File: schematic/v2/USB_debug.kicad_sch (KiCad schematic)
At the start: 16 parts, among them J25 USB_A, J26 APM_DBG, U19 CH340G, Y5 Crystal

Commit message: time to start routing?
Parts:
- removed Y5: Crystal, symbol Device:Crystal
- added Y2: 12MHz, Crystal:Crystal_HC49-4H_Vertical, symbol Device:Crystal
- J26: value APM_DBG -> UART_DEBUG
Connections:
- net at C24.1, U19.7 (XI): now also Y2.1
- net D-: now reaches J25.2 (D-), U19.6 (UD-)
- net D+: now reaches J25.3 (D+), U19.5 (UD+)
- net at C23.1, U19.8 (XO): now also Y2.2
- net APM_DBG_RX renamed USB_DBG_RX
- net USB_DBG_RX: no longer R80.1, R81.1, U19.2 (TXD)
- net APM_DBG_TX renamed DBG_TX
- net DBG_TX: now also R81.1; no longer R81.2
- net APM_VDD renamed USB_DBG_VDD
- new net USB_DBG_TX: R80.1, R81.2, U19.2 (TXD)
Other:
- note added: "UART -> USB Debug Port"
- note added: "USB2.0 DBG PORT"
- note removed: "APM Debug Port"
- note removed: "APM USB2.0 DBG PORT"

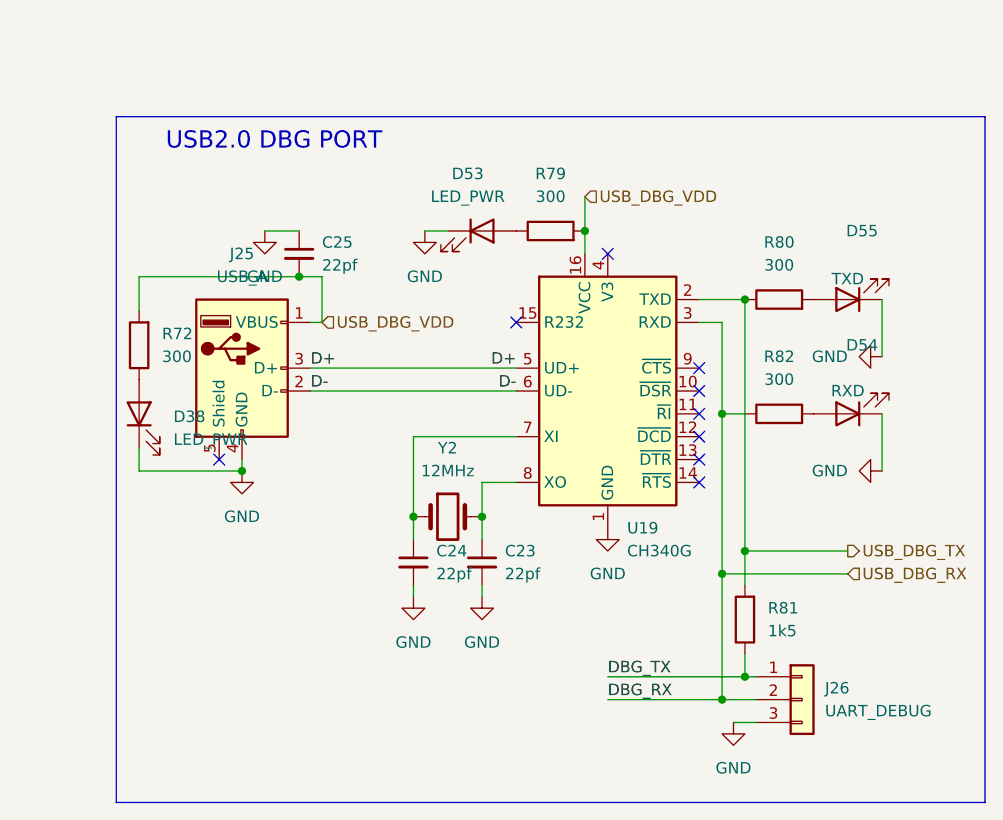
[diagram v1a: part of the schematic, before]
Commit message: dip switch for multi pole filter? this is all for experimenting for now, a refined design with less togleables will come later
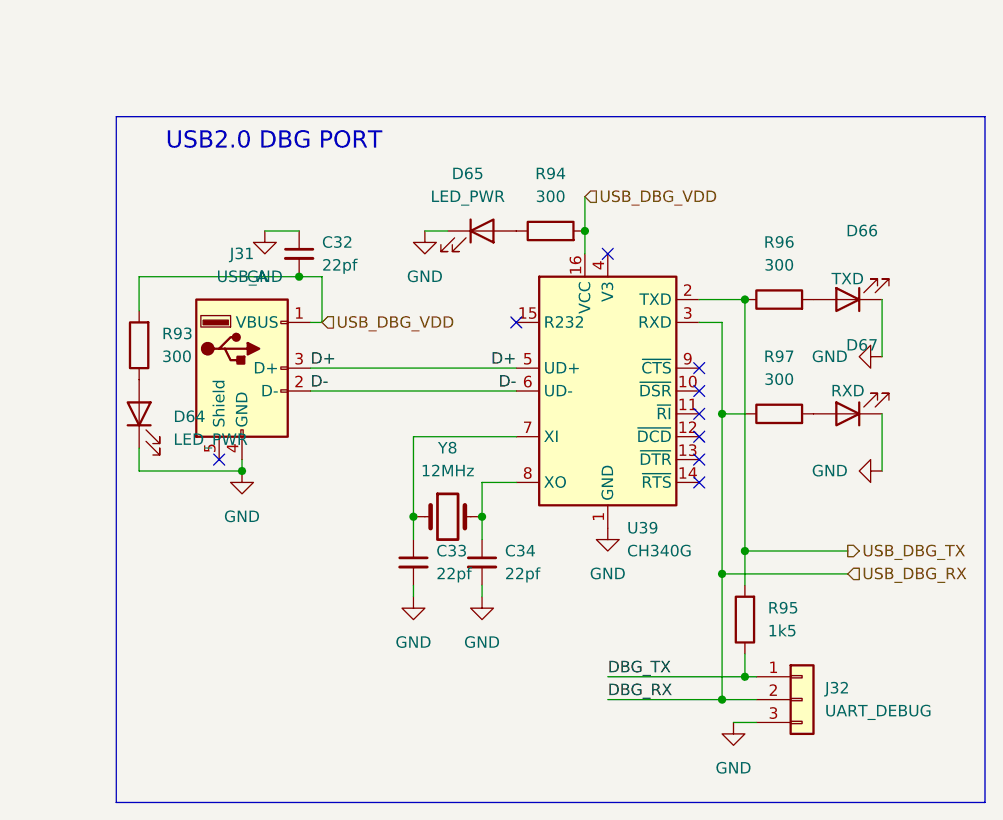
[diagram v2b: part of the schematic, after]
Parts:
- renumbered C25 to C32, C24 to C33, C23 to C34, D38 to D64, D53 to D65, D55 to D66, D54 to D67, J25 to J31, J26 to J32, R72 to R93, R79 to R94, R81 to R95, R80 to R96, R82 to R97, U19 to U39, Y2 to Y8
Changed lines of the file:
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@@
 		(dnp no)
 		(fields_autoplaced yes)
-		(property "Reference" "C25"
+		(property "Reference" "C32"
 			(at 127 67.3162 0)
 			(effects
@@
 		(dnp no)
 		(fields_autoplaced yes)
-		(property "Reference" "Y2"
+		(property "Reference" "Y8"
 			(at 140.97 90.17 0)
 			(effects
@@
 		(dnp no)
 		(fields_autoplaced yes)
-		(property "Reference" "R79"
+		(property "Reference" "R94"
 			(at 152.4 59.69 90)
 			(effects
@@
 		(dnp no)
 		(fields_autoplaced yes)
-		(property "Reference" "C23"
+		(property "Reference" "C34"
 			(at 147.32 101.6062 0)
 			(effects
@@
 		(dnp no)
 		(fields_autoplaced yes)
-		(property "Reference" "C24"
+		(property "Reference" "C33"
 			(at 139.7 101.6062 0)
 			(effects
@@
 		(dnp no)
 		(fields_autoplaced yes)
-		(property "Reference" "#PWR0147"
+		(property "Reference" "#PWR0201"
 			(at 182.88 92.71 0)
 			(effects
@@
 		(dnp no)
 		(fields_autoplaced yes)
-		(property "Reference" "R80"
+		(property "Reference" "R96"
 			(at 177.8 67.31 90)
 			(effects
@@
 		(dnp no)
 		(fields_autoplaced yes)
-		(property "Reference" "#PWR0142"
+		(property "Reference" "#PWR0195"
 			(at 137.16 113.03 0)
 			(effects
@@
 		(dnp no)
 		(fields_autoplaced yes)
-		(property "Reference" "D53"
+		(property "Reference" "D65"
 			(at 143.1925 59.69 0)
 			(effects
@@
 		(dnp no)
 		(fields_autoplaced yes)
-		(property "Reference" "#PWR098"
+		(property "Reference" "#PWR0199"
 			(at 172.72 127 0)
 			(effects
@@
 		(dnp no)
 		(fields_autoplaced yes)
-		(property "Reference" "#PWR0146"
+		(property "Reference" "#PWR0200"
 			(at 182.88 80.01 0)
 			(effects
@@
 		(dnp no)
 		(fields_autoplaced yes)
-		(property "Reference" "#PWR0141"
+		(property "Reference" "#PWR0193"
 			(at 118.11 99.06 0)
 			(effects
@@
 		(dnp no)
 		(fields_autoplaced yes)
-		(property "Reference" "#PWR0144"
+		(property "Reference" "#PWR0197"
 			(at 144.78 113.03 0)
 			(effects
@@
 		(dnp no)
 		(fields_autoplaced yes)
-		(property "Reference" "R82"
+		(property "Reference" "R97"
 			(at 177.8 80.01 90)
 			(effects
@@
 		(dnp no)
 		(fields_autoplaced yes)
-		(property "Reference" "J26"
+		(property "Reference" "J32"
 			(at 182.88 116.8399 0)
 			(effects
@@
 		(dnp no)
 		(fields_autoplaced yes)
-		(property "Reference" "#PWR0145"
+		(property "Reference" "#PWR0198"
 			(at 158.75 105.41 0)
 			(effects
@@
 		(dnp no)
 		(fields_autoplaced yes)
-		(property "Reference" "J25"
+		(property "Reference" "J31"
 			(at 118.11 68.58 0)
 			(effects
@@
 		(dnp no)
 		(fields_autoplaced yes)
-		(property "Reference" "#PWR0143"
+		(property "Reference" "#PWR0196"
 			(at 138.43 72.39 0)
 			(effects
@@
 		(dnp no)
 		(fields_autoplaced yes)
-		(property "Reference" "D38"
+		(property "Reference" "D64"
 			(at 110.49 86.6774 90)
 			(effects
@@
 		(dnp no)
 		(fields_autoplaced yes)
-		(property "Reference" "U19"
+		(property "Reference" "U39"
 			(at 160.8933 99.06 0)
 			(effects
@@
 		(on_board yes)
 		(dnp no)
-		(property "Reference" "D54"
+		(property "Reference" "D67"
 			(at 187.0075 78.74 0)
 			(effects
@@
 		(dnp no)
 		(fields_autoplaced yes)
-		(property "Reference" "#PWR0177"
+		(property "Reference" "#PWR0194"
 			(at 120.65 72.39 0)
 			(effects
@@
 		(dnp no)
 		(fields_autoplaced yes)
-		(property "Reference" "R72"
+		(property "Reference" "R93"
 			(at 109.22 77.4699 0)
 			(effects
@@
 		(on_board yes)
 		(dnp no)
-		(property "Reference" "D55"
+		(property "Reference" "D66"
 			(at 187.0075 66.04 0)
 			(effects
@@
 		(dnp no)
 		(fields_autoplaced yes)
-		(property "Reference" "R81"
+		(property "Reference" "R95"
 			(at 176.53 107.9499 0)
 			(effects
